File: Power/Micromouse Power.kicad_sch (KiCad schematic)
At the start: 37 parts, among them J1 Conn_02x08_Odd_Even, SW1 SW_SPST, U1 TP4056, U2 L9110S, U3 L9110S

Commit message: Added IC lcsc numbers
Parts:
- U1: Availability Not in stock -> (none); Check_prices https://www.snapeda.com/parts/TP4056/NanJing+Top+Power+ASIC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 -> (none); LCSC (none) -> C16581; MANUFACTURER NanJing Top Power ASIC Corp. -> (none); MAXIMUM_PACKAGE_HEIGHT 1.75mm -> (none); MF NanJing Top Power ASIC Corp. -> (none); MP TP4056 -> (none); Package Package -> SOP 8; Populate (none) -> 1; Price None -> (none); STANDARD IPC 7351B -> (none); SnapEDA_Link https://www.snapeda.com/parts/TP4056/NanJing+Top+Power+ASIC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 -> (none)
- U2, U3: Availability Not in stock -> (none); Check_prices https://www.snapeda.com/parts/L9110S/Onsemi/view-part/?ref=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 -> (none); LCSC (none) -> C725793; MANUFACTURER UMW -> (none); MAXIMUM_PACKAGE_HEIGHT 1.7272mm -> (none); MF ON Semiconductor -> (none); MP L9110S -> (none); PARTREV NA -> (none); Populate (none) -> 1; Price None -> (none); STANDARD IPC-7351B -> (none); SnapEDA_Link https://www.snapeda.com/parts/L9110S/Onsemi/view-part/?ref=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 -> (none)
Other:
- moved on the sheet: SW1
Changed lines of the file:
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@@
       (effects (font (size 1.27 1.27)) hide)
-    )
-    (property "MF" "ON Semiconductor" (at 182.245 131.445 0)
-      (effects (font (size 1.27 1.27)) (justify bottom) hide)
-    )
-    (property "MAXIMUM_PACKAGE_HEIGHT" "1.7272mm" (at 182.245 131.445 0)
-      (effects (font (size 1.27 1.27)) (justify bottom) hide)
     )
     (property "Package" "None" (at 182.245 131.445 0)
       (effects (font (size 1.27 1.27)) (justify bottom) hide)
     )
-    (property "Price" "None" (at 182.245 131.445 0)
-      (effects (font (size 1.27 1.27)) (justify bottom) hide)
-    )
-    (property "Check_prices" "https://www.snapeda.com/parts/L9110S/Onsemi/view-part/?ref=eda" (at 182.245 131.445 0)
-      (effects (font (size 1.27 1.27)) (justify bottom) hide)
-    )
-    (property "STANDARD" "IPC-7351B" (at 182.245 131.445 0)
-      (effects (font (size 1.27 1.27)) (justify bottom) hide)
-    )
-    (property "PARTREV" "NA" (at 182.245 131.445 0)
-      (effects (font (size 1.27 1.27)) (justify bottom) hide)
-    )
-    (property "SnapEDA_Link" "https://www.snapeda.com/parts/L9110S/Onsemi/view-part/?ref=snap" (at 182.245 131.445 0)
-      (effects (font (size 1.27 1.27)) (justify bottom) hide)
-    )
-    (property "MP" "L9110S" (at 182.245 131.445 0)
-      (effects (font (size 1.27 1.27)) (justify bottom) hide)
-    )
-    (property "Description" "\nSOP-8 MOTOR DRIVER ICS ROHS\n" (at 182.245 131.445 0)
-      (effects (font (size 1.27 1.27)) (justify bottom) hide)
-    )
-    (property "Availability" "Not in stock" (at 182.245 131.445 0)
-      (effects (font (size 1.27 1.27)) (justify bottom) hide)
-    )
-    (property "MANUFACTURER" "UMW" (at 182.245 131.445 0)
-      (effects (font (size 1.27 1.27)) (justify bottom) hide)
+    (property "LCSC" "C725793" (at 182.245 131.445 0)
+      (effects (font (size 1.27 1.27)) hide)
+    )
+    (property "Populate" "1" (at 182.245 131.445 0)
+      (effects (font (size 1.27 1.27)) hide)
     )
     (pin "5")
@@
       (effects (font (size 1.27 1.27)) hide)
     )
-    (property "MF" "ON Semiconductor" (at 182.245 106.68 0)
-      (effects (font (size 1.27 1.27)) (justify bottom) hide)
-    )
-    (property "MAXIMUM_PACKAGE_HEIGHT" "1.7272mm" (at 182.245 106.68 0)
-      (effects (font (size 1.27 1.27)) (justify bottom) hide)
-    )
     (property "Package" "None" (at 182.245 106.68 0)
       (effects (font (size 1.27 1.27)) (justify bottom) hide)
     )
-    (property "Price" "None" (at 182.245 106.68 0)
-      (effects (font (size 1.27 1.27)) (justify bottom) hide)
-    )
-    (property "Check_prices" "https://www.snapeda.com/parts/L9110S/Onsemi/view-part/?ref=eda" (at 182.245 106.68 0)
-      (effects (font (size 1.27 1.27)) (justify bottom) hide)
-    )
-    (property "STANDARD" "IPC-7351B" (at 182.245 106.68 0)
-      (effects (font (size 1.27 1.27)) (justify bottom) hide)
-    )
-    (property "PARTREV" "NA" (at 182.245 106.68 0)
-      (effects (font (size 1.27 1.27)) (justify bottom) hide)
-    )
-    (property "SnapEDA_Link" "https://www.snapeda.com/parts/L9110S/Onsemi/view-part/?ref=snap" (at 182.245 106.68 0)
-      (effects (font (size 1.27 1.27)) (justify bottom) hide)
-    )
-    (property "MP" "L9110S" (at 182.245 106.68 0)
-      (effects (font (size 1.27 1.27)) (justify bottom) hide)
-    )
-    (property "Description" "\nSOP-8 MOTOR DRIVER ICS ROHS\n" (at 182.245 106.68 0)
-      (effects (font (size 1.27 1.27)) (justify bottom) hide)
-    )
-    (property "Availability" "Not in stock" (at 182.245 106.68 0)
-      (effects (font (size 1.27 1.27)) (justify bottom) hide)
-    )
-    (property "MANUFACTURER" "UMW" (at 182.245 106.68 0)
-      (effects (font (size 1.27 1.27)) (justify bottom) hide)
+    (property "LCSC" "C725793" (at 182.245 106.68 0)
+      (effects (font (size 1.27 1.27)) hide)
+    )
+    (property "Populate" "1" (at 182.245 106.68 0)
+      (effects (font (size 1.27 1.27)) hide)
     )
     (pin "5")
@@
     )
   )
-  (symbol (lib_id "Switch:SW_SPST") (at 300.355 28.575 0) (unit 1)
+  (symbol (lib_id "Switch:SW_SPST") (at 123.825 114.3 0) (unit 1)
     (in_bom yes) (on_board yes) (dnp no) (fields_autoplaced)
-    (property "Reference" "SW1" (at 300.355 22.479 0)
-      (effects (font (size 1.27 1.27)))
-    )
-    (property "Value" "SW_SPST" (at 300.355 25.019 0)
-      (effects (font (size 1.27 1.27)))
-    )
-    (property "Footprint" "" (at 300.355 28.575 0)
-      (effects (font (size 1.27 1.27)) hide)
-    )
-    (property "Datasheet" "~" (at 300.355 28.575 0)
+    (property "Reference" "SW1" (at 123.825 108.204 0)
+      (effects (font (size 1.27 1.27)))
+    )
+    (property "Value" "SW_SPST" (at 123.825 110.744 0)
+      (effects (font (size 1.27 1.27)))
+    )
+    (property "Footprint" "" (at 123.825 114.3 0)
+      (effects (font (size 1.27 1.27)) hide)
+    )
+    (property "Datasheet" "~" (at 123.825 114.3 0)
       (effects (font (size 1.27 1.27)) hide)
     )
@@
       (effects (font (size 1.27 1.27)) hide)
     )
-    (property "MF" "NanJing Top Power ASIC Corp." (at 96.52 87.63 0)
+    (property "Package" "SOP 8" (at 96.52 87.63 0)
       (effects (font (size 1.27 1.27)) (justify bottom) hide)
     )
-    (property "MAXIMUM_PACKAGE_HEIGHT" "1.75mm" (at 96.52 87.63 0)
-      (effects (font (size 1.27 1.27)) (justify bottom) hide)
-    )
-    (property "Package" "Package" (at 96.52 87.63 0)
-      (effects (font (size 1.27 1.27)) (justify bottom) hide)
-    )
-    (property "Price" "None" (at 96.52 87.63 0)
-      (effects (font (size 1.27 1.27)) (justify bottom) hide)
-    )
-    (property "Check_prices" "https://www.snapeda.com/parts/TP4056/NanJing+Top+Power+ASIC+Corp./view-part/?ref=eda" (at 96.52 87.63 0) (show_name)
-      (effects (font (size 1.27 1.27)) (justify bottom) hide)
-    )
-    (property "STANDARD" "IPC 7351B" (at 96.52 87.63 0)
-      (effects (font (size 1.27 1.27)) (justify bottom) hide)
-    )
-    (property "SnapEDA_Link" "https://www.snapeda.com/parts/TP4056/NanJing+Top+Power+ASIC+Corp./view-part/?ref=snap" (at 96.52 87.63 0)
-      (effects (font (size 1.27 1.27)) (justify bottom) hide)
-    )
-    (property "MP" "TP4056" (at 96.52 87.63 0)
-      (effects (font (size 1.27 1.27)) (justify bottom) hide)
-    )
-    (property "Description" "\nComplete single cell Li-Ion battery with a constant current / constant voltage linear charger\n" (at 96.52 87.63 0)
-      (effects (font (size 1.27 1.27)) (justify bottom) hide)
-    )
-    (property "Availability" "Not in stock" (at 96.52 87.63 0)
-      (effects (font (size 1.27 1.27)) (justify bottom) hide)
-    )
-    (property "MANUFACTURER" "NanJing Top Power ASIC Corp." (at 96.52 87.63 0)
-      (effects (font (size 1.27 1.27)) (justify bottom) hide)
+    (property "LCSC" "C16581" (at 96.52 87.63 0)
+      (effects (font (size 1.27 1.27)) hide)
+    )
+    (property "Populate" "1" (at 96.52 87.63 0)
+      (effects (font (size 1.27 1.27)) hide)
     )
     (pin "8")

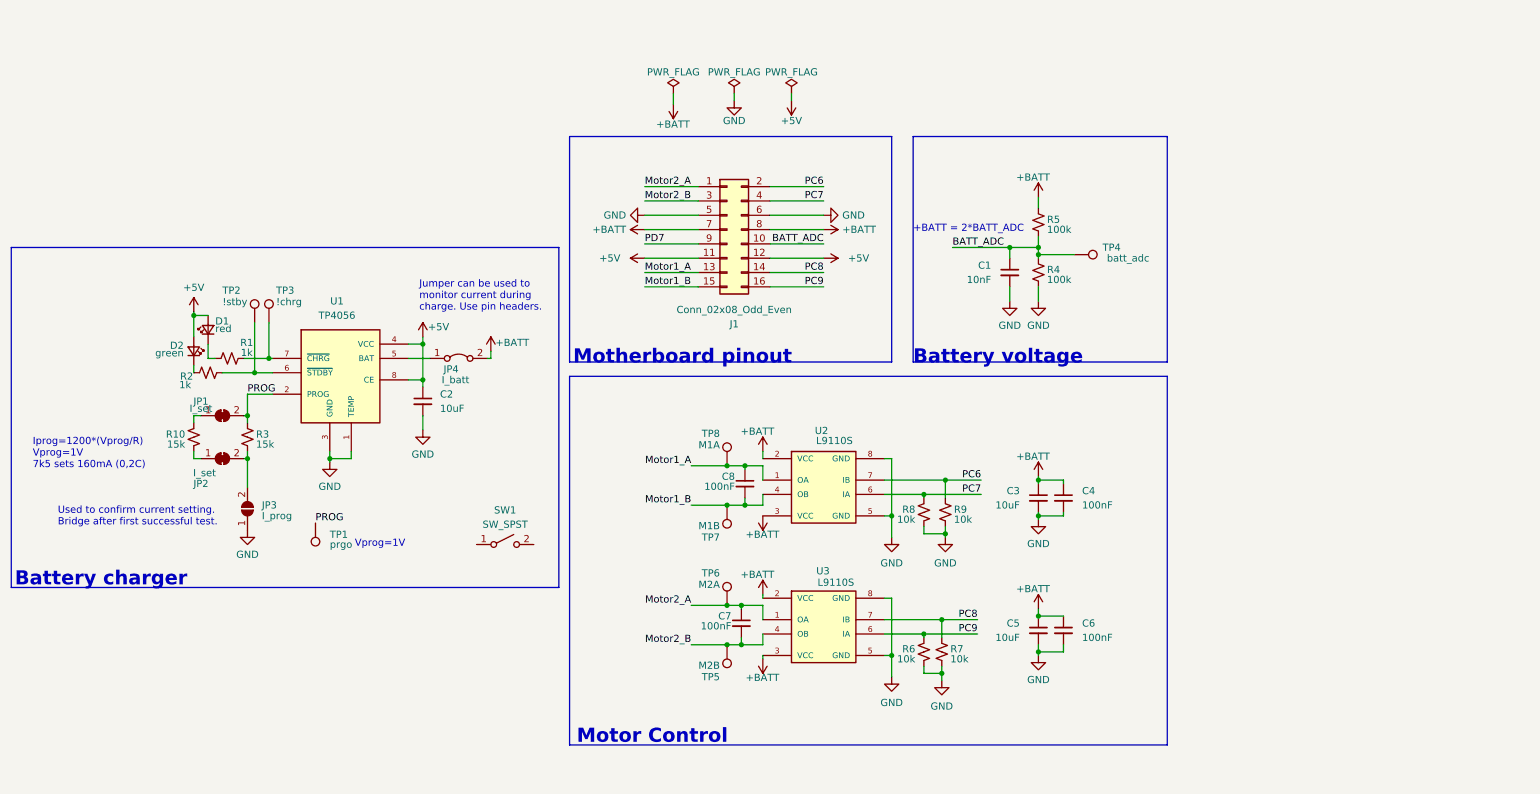
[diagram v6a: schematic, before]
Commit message: Added switched +batt
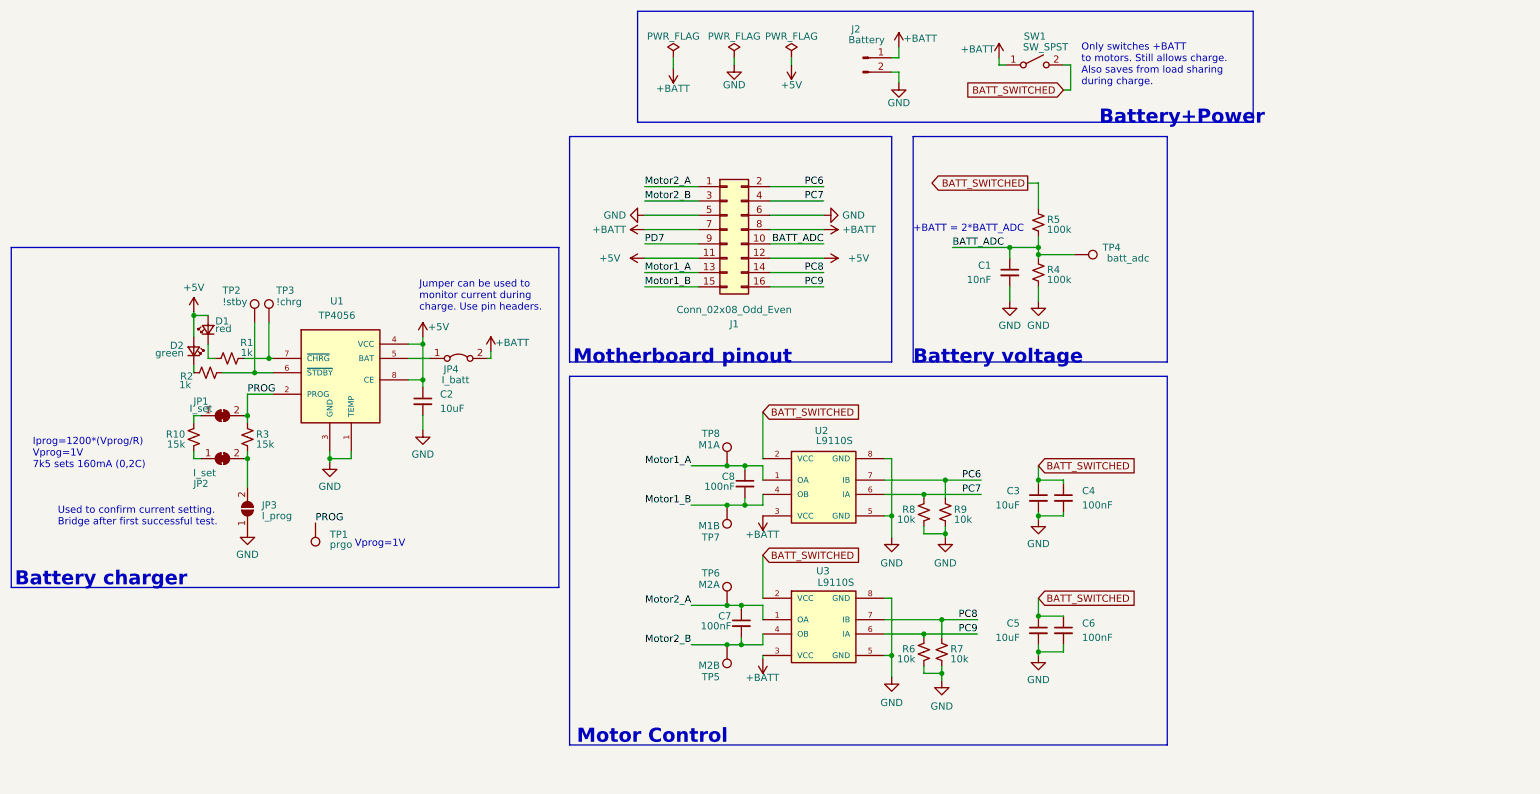
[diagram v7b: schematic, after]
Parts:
- added J2: Battery, Connector_JST:JST_PH_B2B-PH-K_1x02_P2.00mm_Vertical, symbol Connector:Conn_01x02_Pin
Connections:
- net +BATT: now also SW1.1 (A), J2.1 (Pin_1); no longer C3.1, C4.1, C5.1, C6.1, R5.2, U2.2 (VCC), U3.2 (VCC)
- net GND: now also J2.2 (Pin_2)
- net BATT_SWITCHED: now reaches SW1.2 (B)
- net BATT_SWITCHED: now also C3.1, C4.1, C5.1, C6.1, R5.2, U2.2 (VCC), U3.2 (VCC)
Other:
- note added: "Battery+Power"
- note added: "Only switches +BATT to motors. Still allows charge. Also saves from load sharing during charge."
- moved on the sheet: SW1

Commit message: Changed motor IC to drv8837
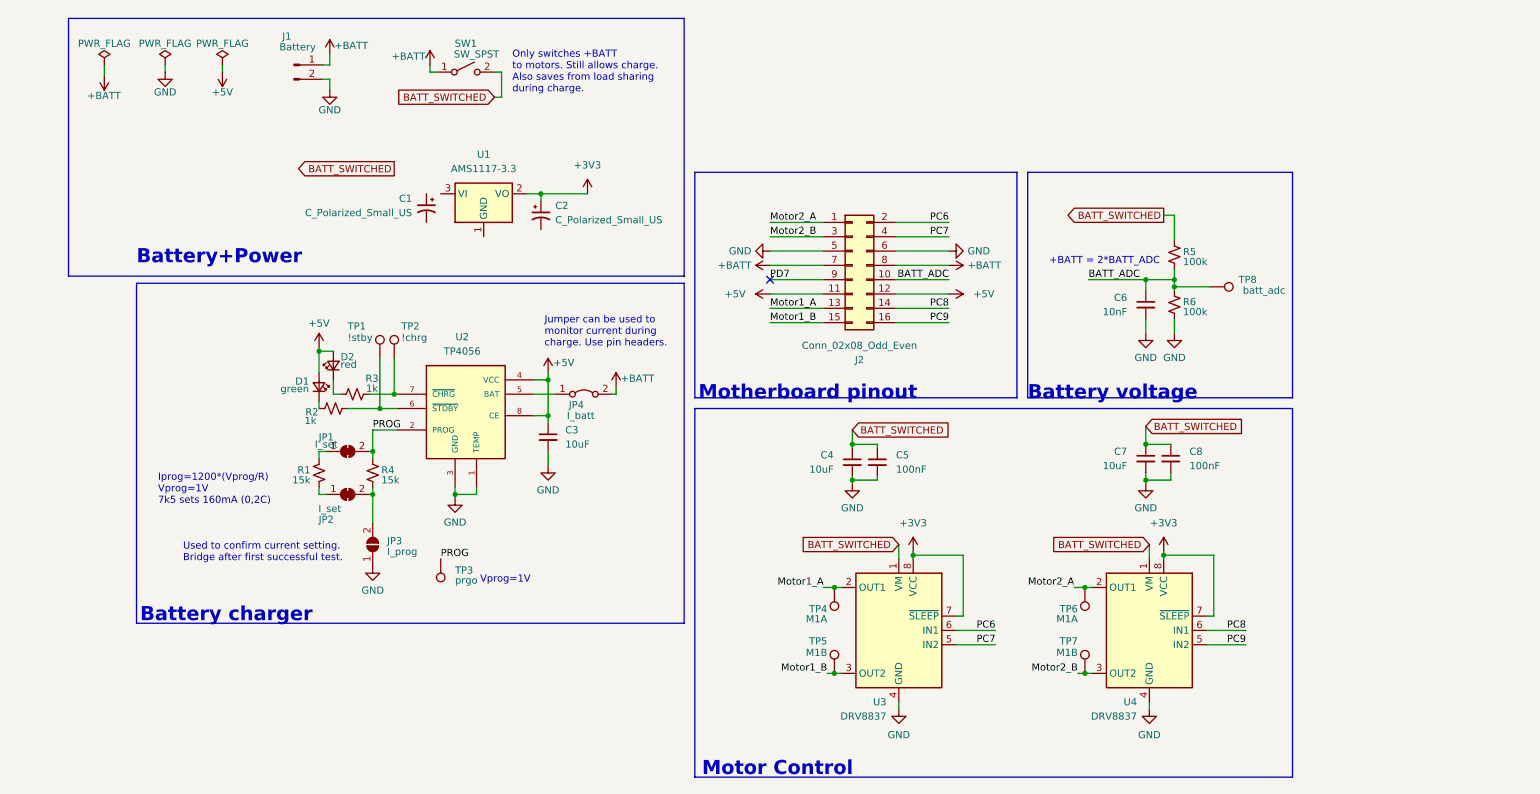
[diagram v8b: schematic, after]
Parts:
- removed C7, C8: 100nF, symbol Device:C_Small
- removed R6, R7, R8, R9: 10k, symbol Device:R_Small_US
- removed TP5: M2B, TestPoint:TestPoint_Pad_D1.0mm, symbol Connector:TestPoint
- removed U2, U3: L9110S, L9110S:SOIC127P599X172-8N, symbol L9110S:L9110S
- added C1, C2: C_Polarized_Small_US, symbol Device:C_Polarized_Small_US
- added TP7: M1B, TestPoint:TestPoint_Pad_D1.0mm, symbol Connector:TestPoint
- added U1: AMS1117-3.3, Package_TO_SOT_SMD:SOT-223-3_TabPin2, symbol Regulator_Linear:AMS1117-3.3
- added U3, U4: DRV8837, Package_SON:WSON-8-1EP_2x2mm_P0.5mm_EP0.9x1.6mm, symbol Driver_Motor:DRV8837
- TP6: value M2A -> M1A
- renumbered C2 to C3, C3 to C4, C4 to C5, C1 to C6, C5 to C7, C6 to C8, D2 to D1, D1 to D2, J2 to J1, J1 to J2, R10 to R1, R1 to R3, R3 to R4, R4 to R6, TP2 to TP1, TP3 to TP2, TP1 to TP3, TP8 to TP4, TP7 to TP5, TP4 to TP8, U1 to U2
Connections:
- net BATT_SWITCHED: now also U3.1 (VM), U4.1 (VM)
- net GND: now also U3.4 (GND), U3.9 (GND), U4.4 (GND), U4.9 (GND)
- net Motor1_A: now also U3.2 (OUT1)
- net Motor1_B: now also U3.3 (OUT2)
- net Motor2_A: now also U4.2 (OUT1)
- net Motor2_B: now also TP7.1, U4.3 (OUT2)
- net PC6: now also U3.6 (IN1)
- net PC7: now also U3.5 (IN2)
- net PC8: now also U4.6 (IN1)
- net PC9: now also U4.5 (IN2)
- new net +3V3: C2.1, U1.2 (VO), U3.7 (~{SLEEP}), U3.8 (VCC), U4.7 (~{SLEEP}), U4.8 (VCC)
- no-connect marks 0 -> 1
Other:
- moved on the sheet: C3, C4, C5, C6, C7, C8, D1, D2, J1, J2, JP1, JP2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
